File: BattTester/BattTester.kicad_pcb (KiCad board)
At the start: 2 copper layers, 99.7 x 63.5 mm, 30 parts, among them J1 Battery, J2 SD_Card, J3 PWR, J4 UPDI, Q1 IRLZ44N, Q2 IRF4905, Q3 2N7002, U1 LTC1286CN8, U2 ATtiny1624-SS, U3 LD1086DT33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

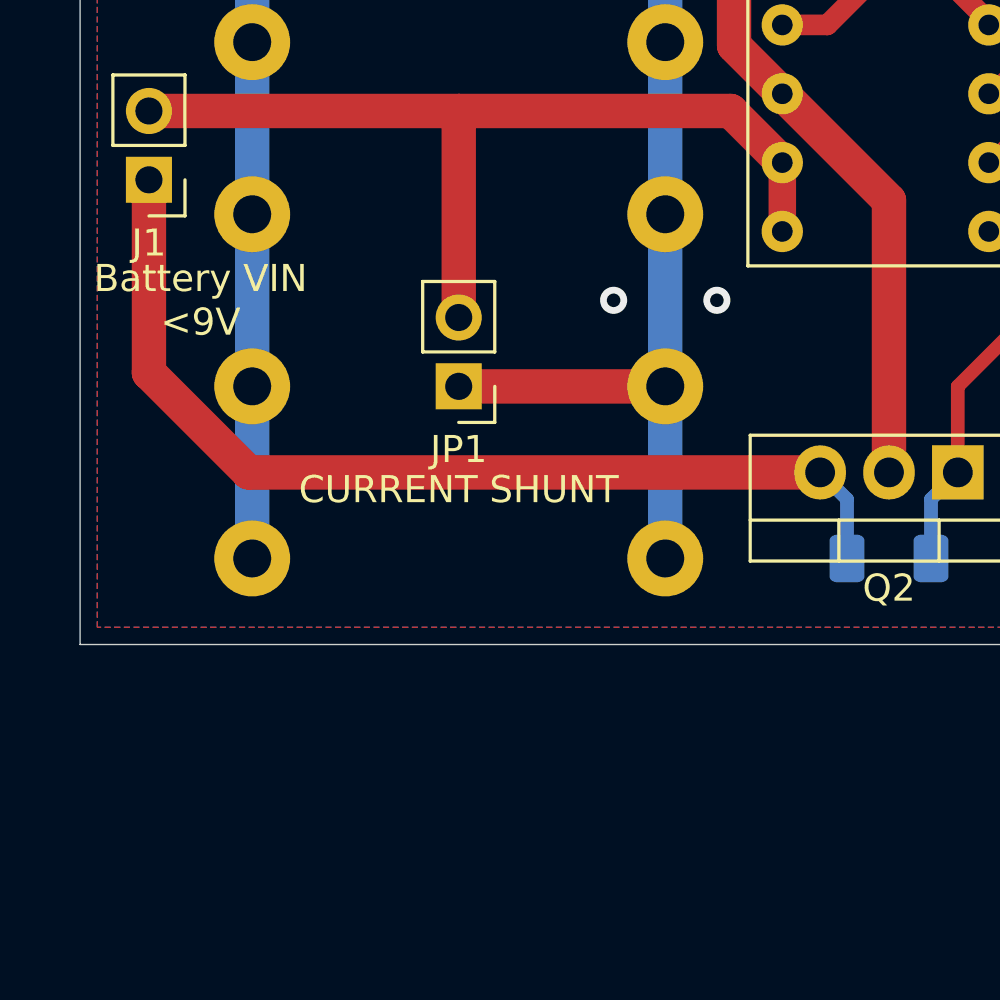
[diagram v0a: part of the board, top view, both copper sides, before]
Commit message: add current sense
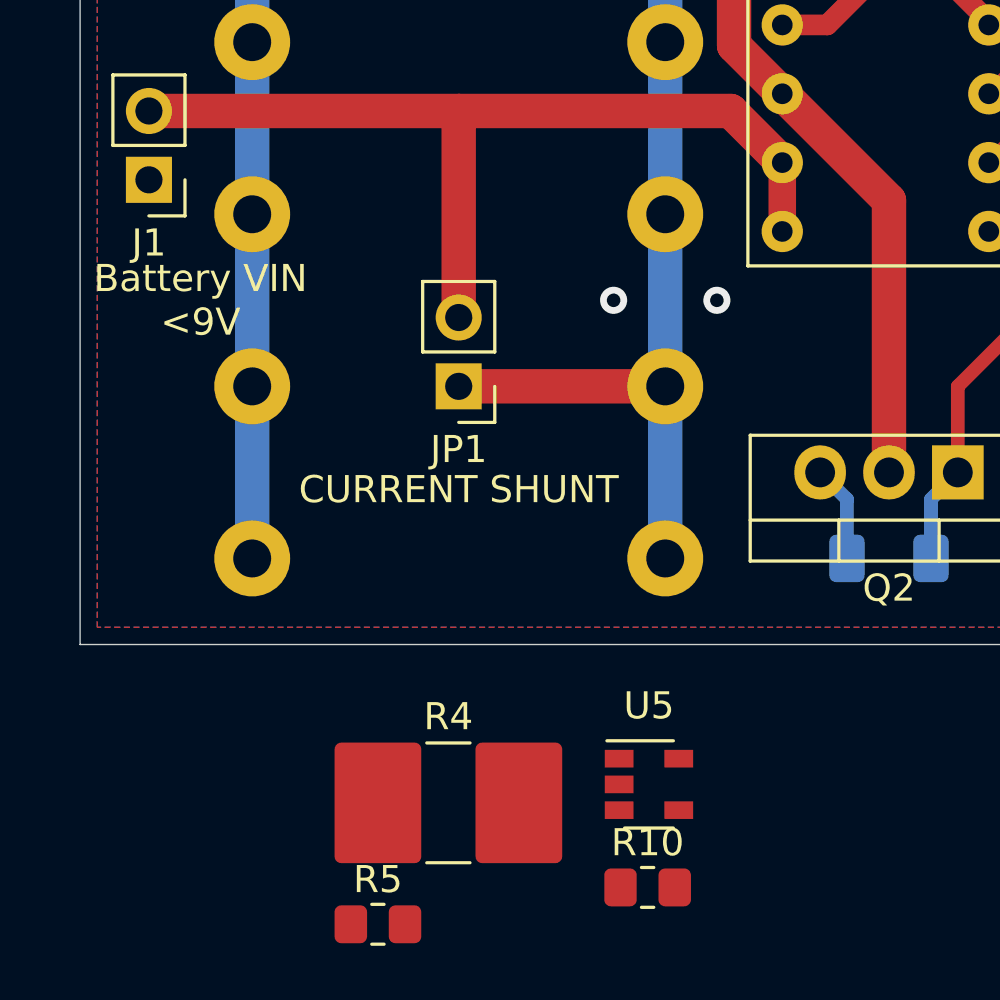
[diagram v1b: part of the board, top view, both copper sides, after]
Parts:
- added R10: 2K, Resistor_SMD:R_0805_2012Metric_Pad1.20x1.40mm_HandSolder, F.Cu at (160.0, 136.0)
- added R4: 10m, Resistor_SMD:R_2816_7142Metric_Pad3.20x4.45mm_HandSolder, F.Cu at (152.7, 132.8)
- added R5: 100R, Resistor_SMD:R_0805_2012Metric_Pad1.20x1.40mm_HandSolder, F.Cu at (150.1, 137.3)
- added U5: LT6106, Package_TO_SOT_SMD:SOT-23-5, F.Cu at (160.1, 132.2)
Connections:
- J1 pad 1: /BIN+ -> /ISH+
- Q2 pad 3: /BIN+ -> /ISH-
- R7 pad 2: /BIN+ -> /ISH-
- U2 pad 5: (no net) -> /I_OUT
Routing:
- net /BIN+: track 37.0 -> 0.00 mm
- net /ISH-: track 0.00 -> 3.59 mm

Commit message: finished routing
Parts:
- U3: value LD1086DT33 -> LM1117-3.3; footprint Package_TO_SOT_SMD:TO-252-3_TabPin2 -> Package_TO_SOT_THT:TO-220-3_Vertical
- moved U3 19.8 mm to (194.1, 69.0), turned to 0 degrees
- moved D3 18.7 mm to (201.2, 86.4), turned to 180 degrees
- moved R4 15.0 mm to (152.8, 117.9)
- moved R5 11.5 mm to (148.3, 126.0), turned to 90 degrees
- moved U5 10.5 mm to (152.9, 124.5), turned to 90 degrees
- moved J3 10.2 mm to (198.1, 79.8), turned to 270 degrees
- moved R10 9.31 mm to (157.5, 127.0), turned to 90 degrees
- moved C5 8.27 mm to (200.2, 75.2)
- moved Q2 7.11 mm to (178.6, 120.7)
- moved R7 7.11 mm to (176.0, 123.8)
- moved C6 6.20 mm to (195.6, 75.2), turned to 180 degrees
- moved JP1 5.21 mm to (152.9, 112.3)
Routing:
- net /I_OUT: track 0.00 -> 69.4 mm, vias 0 -> 2
- net /ISH-: track 3.59 -> 28.9 mm
- net /ISH+: track 0.00 -> 23.5 mm
- net Net-(Q2-Pad1): track 24.3 -> 8.17 mm
- net +9V: track 103.9 -> 118.8 mm
- net GND: track 63.0 -> 49.0 mm, vias 8 -> 11
- net Net-(R5-Pad1): track 0.00 -> 7.42 mm
- net +3V3: track 122.0 -> 126.7 mm, vias 0 -> 1
- net /B+: track 63.1 -> 66.0 mm
- net Net-(JP1-Pad1): track 64.8 -> 65.4 mm
- net /CUTOFF: track 22.5 -> 23.0 mm
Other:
- board size 99.7 x 63.5 mm -> 99.7 x 66 mm

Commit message: add test point
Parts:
- added TP1: Current measurement, Connector_PinHeader_2.54mm:PinHeader_1x02_P2.54mm_Vertical, F.Cu at (167.1, 128.0)

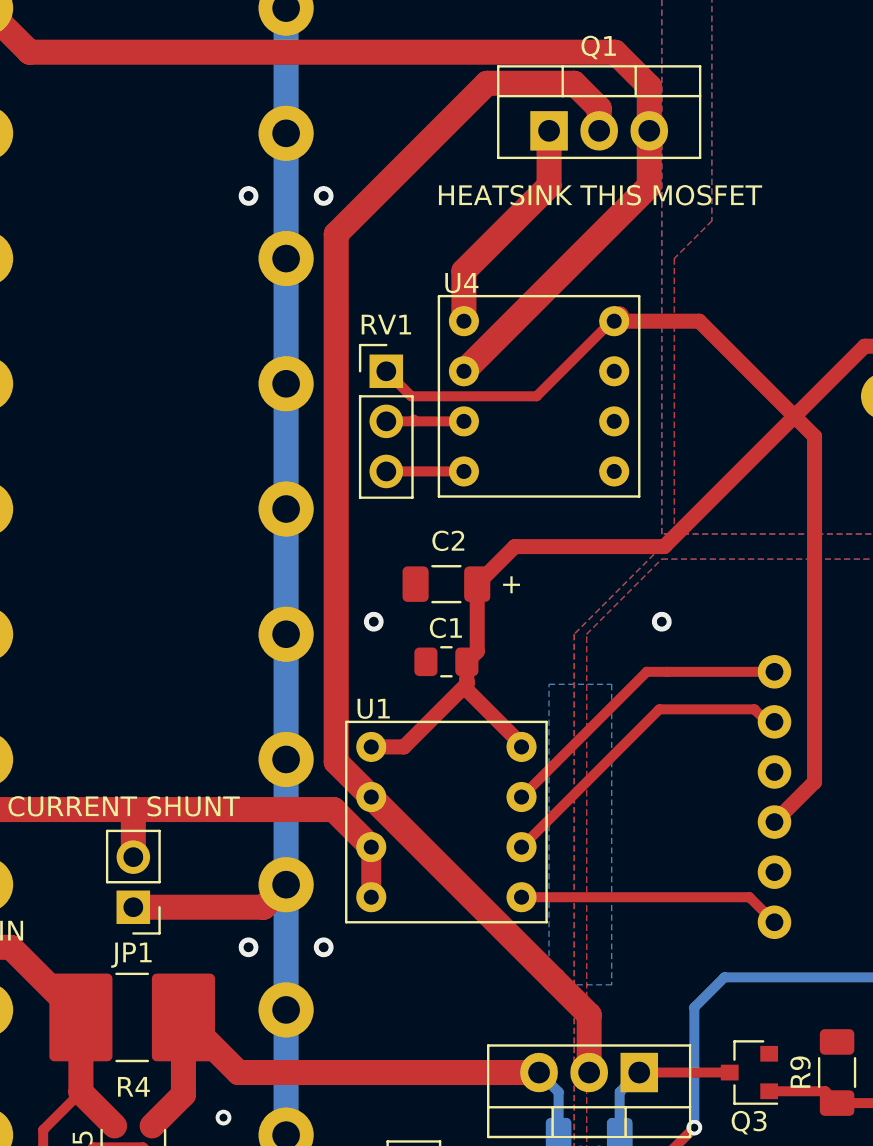
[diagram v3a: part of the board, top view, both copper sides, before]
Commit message: standardize dip-8, tie off second lm358 output
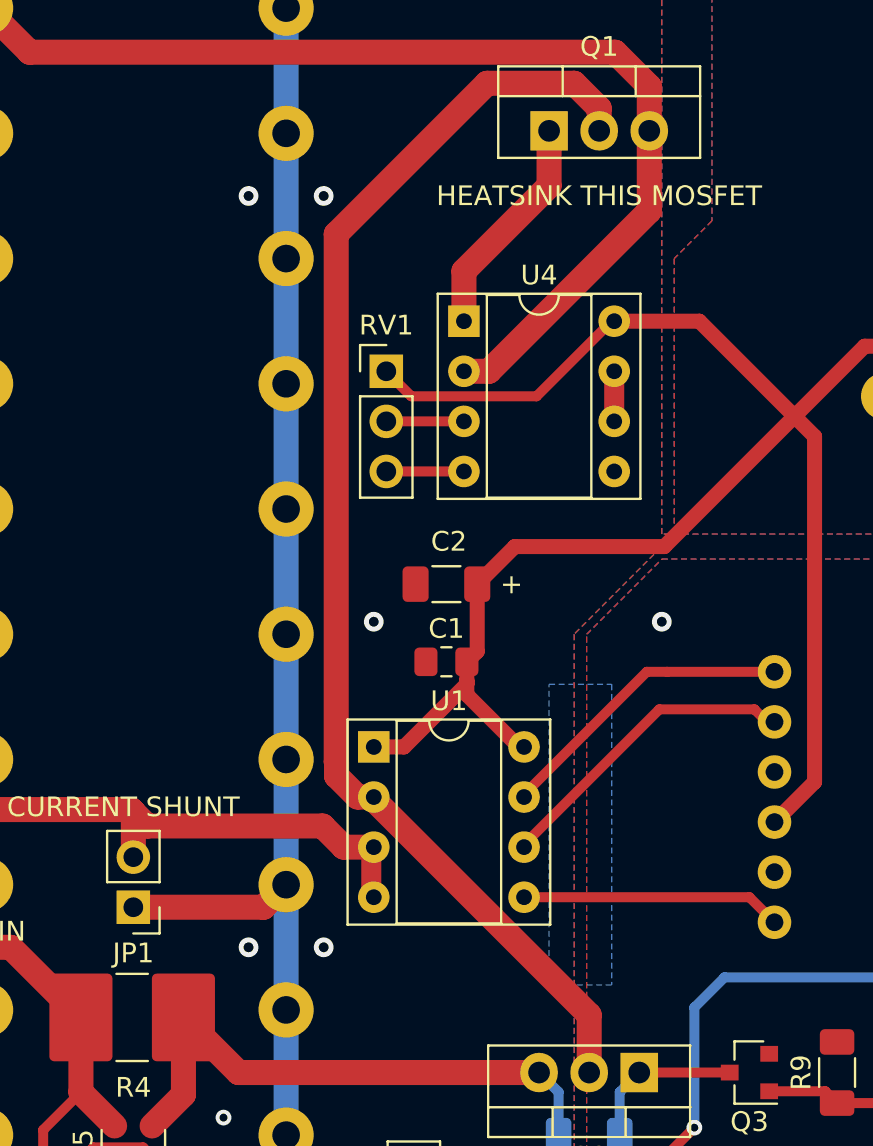
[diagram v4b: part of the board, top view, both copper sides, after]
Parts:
- U1: footprint BattTester:DIP8 -> Package_DIP:DIP-8_W7.62mm_Socket
- U4: value LM358AN -> LM358; footprint BattTester:DIP8 -> Package_DIP:DIP-8_W7.62mm_Socket
- moved U4 4.02 mm to (169.7, 82.5)
- moved U1 3.90 mm to (165.1, 104.1)
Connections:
- U4 pad 5: (no net) -> GND
- U4 pad 6: (no net) -> Net-(U4-Pad6)
- U4 pad 7: (no net) -> Net-(U4-Pad6)
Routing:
- net Net-(U4-Pad6): track 0.00 -> 2.54 mm
- net Net-(Q1-Pad3): track 110.8 -> 111.5 mm
